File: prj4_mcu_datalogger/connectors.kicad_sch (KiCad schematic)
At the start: 4 parts, among them J1 Conn_01x04_Pin, J2 Conn_01x04_Pin, J3 Conn_01x09_Pin, J4 Conn_02x03_Odd_Even

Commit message: Associazione simboli/footprint
Feat: associati i simboli dei componenti con i relativi footprint
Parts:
- J1, J2: footprint (none) -> Connector_PinHeader_2.54mm:PinHeader_1x04_P2.54mm_Vertical
- J3: footprint (none) -> Connector_PinHeader_2.54mm:PinHeader_1x09_P2.54mm_Vertical
- J4: footprint (none) -> Connector_PinHeader_2.54mm:PinHeader_2x03_P2.54mm_Vertical
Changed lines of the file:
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@@
       (effects (font (size 1.27 1.27)))
     )
-    (property "Footprint" "" (at 121.92 73.66 0)
+    (property "Footprint" "Connector_PinHeader_2.54mm:PinHeader_1x04_P2.54mm_Vertical" (at 121.92 73.66 0)
       (effects (font (size 1.27 1.27)) hide)
     )
@@
       (effects (font (size 1.27 1.27)))
     )
-    (property "Footprint" "" (at 121.92 109.22 0)
+    (property "Footprint" "Connector_PinHeader_2.54mm:PinHeader_1x09_P2.54mm_Vertical" (at 121.92 109.22 0)
       (effects (font (size 1.27 1.27)) hide)
     )
@@
       (effects (font (size 1.27 1.27)))
     )
-    (property "Footprint" "" (at 165.1 109.22 0)
+    (property "Footprint" "Connector_PinHeader_2.54mm:PinHeader_2x03_P2.54mm_Vertical" (at 165.1 109.22 0)
       (effects (font (size 1.27 1.27)) hide)
     )
@@
       (effects (font (size 1.27 1.27)))
     )
-    (property "Footprint" "" (at 165.1 73.66 0)
+    (property "Footprint" "Connector_PinHeader_2.54mm:PinHeader_1x04_P2.54mm_Vertical" (at 165.1 73.66 0)
       (effects (font (size 1.27 1.27)) hide)
     )

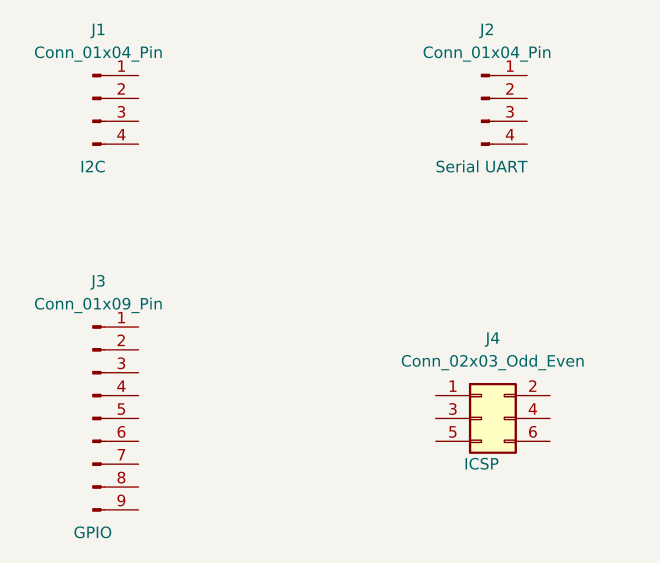
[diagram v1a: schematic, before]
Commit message: Completate le connessioni nello schematico
Feat: connessi tutti i pin in entrambi i fogli
Feat: effettuato ERC
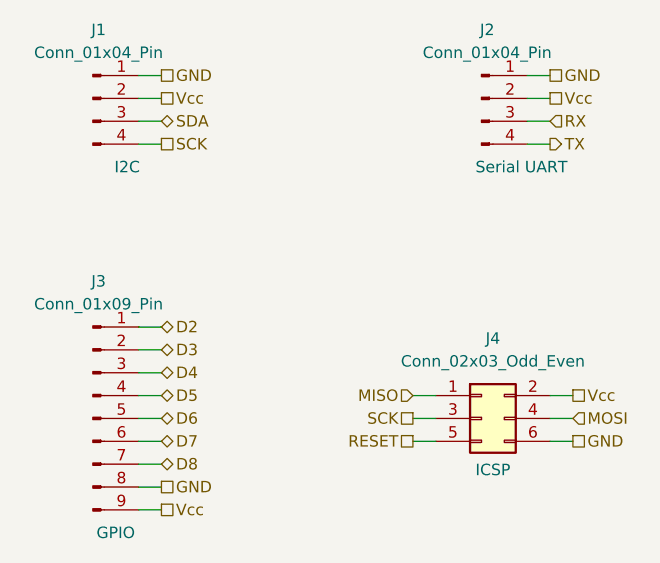
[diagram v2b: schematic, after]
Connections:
- net GND: now reaches J1.1 (Pin_1)
- net GND: now also J2.1 (Pin_1), J3.8 (Pin_8), J4.6 (Pin_6)
- net Vcc: now reaches J1.2 (Pin_2)
- net Vcc: now also J2.2 (Pin_2), J3.9 (Pin_9), J4.2 (Pin_2)
- net SDA: now reaches J1.3 (Pin_3)
- net SCK: now reaches J1.4 (Pin_4)
- net SCK: now also J4.3 (Pin_3)
- net D2: now reaches J3.1 (Pin_1)
- net D3: now reaches J3.2 (Pin_2)
- net D4: now reaches J3.3 (Pin_3)
- net D5: now reaches J3.4 (Pin_4)
- net D6: now reaches J3.5 (Pin_5)
- net D7: now reaches J3.6 (Pin_6)
- net D8: now reaches J3.7 (Pin_7)
- net MISO: now reaches J4.1 (Pin_1)
- net MOSI: now reaches J4.4 (Pin_4)
- net RESET: now reaches J4.5 (Pin_5)
- net RX: now reaches J2.3 (Pin_3)
- net TX: now reaches J2.4 (Pin_4)
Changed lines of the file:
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@@
 (kicad_sch (version 20230121) (generator eeschema)
   (paper "A4")
+  (wire (pts (xy 127 109.22) (xy 129.54 109.22))
+    (stroke (width 0) (type default))
+  )
+  (wire (pts (xy 127 78.74) (xy 129.54 78.74))
+    (stroke (width 0) (type default))
+  )
+  (wire (pts (xy 127 73.66) (xy 129.54 73.66))
+    (stroke (width 0) (type default))
+  )
+  (wire (pts (xy 170.18 78.74) (xy 172.72 78.74))
+    (stroke (width 0) (type default))
+  )
+  (wire (pts (xy 172.72 111.76) (xy 175.26 111.76))
+    (stroke (width 0) (type default))
+  )
+  (wire (pts (xy 170.18 71.12) (xy 172.72 71.12))
+    (stroke (width 0) (type default))
+  )
+  (wire (pts (xy 127 106.68) (xy 129.54 106.68))
+    (stroke (width 0) (type default))
+  )
+  (wire (pts (xy 127 76.2) (xy 129.54 76.2))
+    (stroke (width 0) (type default))
+  )
+  (wire (pts (xy 127 99.06) (xy 129.54 99.06))
+    (stroke (width 0) (type default))
+  )
+  (wire (pts (xy 127 116.84) (xy 129.54 116.84))
+    (stroke (width 0) (type default))
+  )
+  (wire (pts (xy 127 71.12) (xy 129.54 71.12))
+    (stroke (width 0) (type default))
+  )
+  (wire (pts (xy 157.48 111.76) (xy 160.02 111.76))
+    (stroke (width 0) (type default))
+  )
+  (wire (pts (xy 170.18 76.2) (xy 172.72 76.2))
+    (stroke (width 0) (type default))
+  )
+  (wire (pts (xy 157.48 109.22) (xy 160.02 109.22))
+    (stroke (width 0) (type default))
+  )
+  (wire (pts (xy 127 111.76) (xy 129.54 111.76))
+    (stroke (width 0) (type default))
+  )
+  (wire (pts (xy 127 119.38) (xy 129.54 119.38))
+    (stroke (width 0) (type default))
+  )
+  (wire (pts (xy 127 104.14) (xy 129.54 104.14))
+    (stroke (width 0) (type default))
+  )
+  (wire (pts (xy 172.72 106.68) (xy 175.26 106.68))
+    (stroke (width 0) (type default))
+  )
+  (wire (pts (xy 157.48 106.68) (xy 160.02 106.68))
+    (stroke (width 0) (type default))
+  )
+  (wire (pts (xy 127 114.3) (xy 129.54 114.3))
+    (stroke (width 0) (type default))
+  )
+  (wire (pts (xy 127 101.6) (xy 129.54 101.6))
+    (stroke (width 0) (type default))
+  )
+  (wire (pts (xy 172.72 109.22) (xy 175.26 109.22))
+    (stroke (width 0) (type default))
+  )
+  (wire (pts (xy 170.18 73.66) (xy 172.72 73.66))
+    (stroke (width 0) (type default))
+  )
+  (hierarchical_label "GND" (shape passive) (at 129.54 71.12 0) (fields_autoplaced)
+    (effects (font (size 1.27 1.27)) (justify left))
+  )
+  (hierarchical_label "GND" (shape passive) (at 175.26 111.76 0) (fields_autoplaced)
+    (effects (font (size 1.27 1.27)) (justify left))
+  )
+  (hierarchical_label "RX" (shape input) (at 172.72 76.2 0) (fields_autoplaced)
+    (effects (font (size 1.27 1.27)) (justify left))
+  )
+  (hierarchical_label "SCK" (shape passive) (at 129.54 78.74 0) (fields_autoplaced)
+    (effects (font (size 1.27 1.27)) (justify left))
+  )
+  (hierarchical_label "D3" (shape bidirectional) (at 129.54 101.6 0) (fields_autoplaced)
+    (effects (font (size 1.27 1.27)) (justify left))
+  )
+  (hierarchical_label "GND" (shape passive) (at 172.72 71.12 0) (fields_autoplaced)
+    (effects (font (size 1.27 1.27)) (justify left))
+  )
+  (hierarchical_label "D5" (shape bidirectional) (at 129.54 106.68 0) (fields_autoplaced)
+    (effects (font (size 1.27 1.27)) (justify left))
+  )
+  (hierarchical_label "Vcc" (shape passive) (at 175.26 106.68 0) (fields_autoplaced)
+    (effects (font (size 1.27 1.27)) (justify left))
+  )
+  (hierarchical_label "D8" (shape bidirectional) (at 129.54 114.3 0) (fields_autoplaced)
+    (effects (font (size 1.27 1.27)) (justify left))
+  )
+  (hierarchical_label "SCK" (shape passive) (at 157.48 109.22 180) (fields_autoplaced)
+    (effects (font (size 1.27 1.27)) (justify right))
+  )
+  (hierarchical_label "Vcc" (shape passive) (at 129.54 119.38 0) (fields_autoplaced)
+    (effects (font (size 1.27 1.27)) (justify left))
+  )
+  (hierarchical_label "GND" (shape passive) (at 129.54 116.84 0) (fields_autoplaced)
+    (effects (font (size 1.27 1.27)) (justify left))
+  )
+  (hierarchical_label "D7" (shape bidirectional) (at 129.54 111.76 0) (fields_autoplaced)
+    (effects (font (size 1.27 1.27)) (justify left))
+  )
+  (hierarchical_label "Vcc" (shape passive) (at 172.72 73.66 0) (fields_autoplaced)
+    (effects (font (size 1.27 1.27)) (justify left))
+  )
+  (hierarchical_label "MISO" (shape input) (at 157.48 106.68 180) (fields_autoplaced)
+    (effects (font (size 1.27 1.27)) (justify right))
+  )
+  (hierarchical_label "Vcc" (shape passive) (at 129.54 73.66 0) (fields_autoplaced)
+    (effects (font (size 1.27 1.27)) (justify left))
+  )
+  (hierarchical_label "D2" (shape bidirectional) (at 129.54 99.06 0) (fields_autoplaced)
+    (effects (font (size 1.27 1.27)) (justify left))
+  )
+  (hierarchical_label "D4" (shape bidirectional) (at 129.54 104.14 0) (fields_autoplaced)
+    (effects (font (size 1.27 1.27)) (justify left))
+  )
+  (hierarchical_label "SDA" (shape bidirectional) (at 129.54 76.2 0) (fields_autoplaced)
+    (effects (font (size 1.27 1.27)) (justify left))
+  )
+  (hierarchical_label "RESET" (shape passive) (at 157.48 111.76 180) (fields_autoplaced)
+    (effects (font (size 1.27 1.27)) (justify right))
+  )
+  (hierarchical_label "MOSI" (shape input) (at 175.26 109.22 0) (fields_autoplaced)
+    (effects (font (size 1.27 1.27)) (justify left))
+  )
+  (hierarchical_label "TX" (shape output) (at 172.72 78.74 0) (fields_autoplaced)
+    (effects (font (size 1.27 1.27)) (justify left))
+  )
+  (hierarchical_label "D6" (shape bidirectional) (at 129.54 109.22 0) (fields_autoplaced)
+    (effects (font (size 1.27 1.27)) (justify left))
+  )
   (symbol (lib_id "Connector:Conn_01x04_Pin") (at 121.92 73.66 0) (unit 1)
     (in_bom yes) (on_board yes) (dnp no)
@@
       (effects (font (size 1.27 1.27)) hide)
     )
-    (property "Purpose" "I2C" (at 121.92 81.28 0)
+    (property "Purpose" "I2C" (at 125.73 81.28 0)
       (effects (font (size 1.27 1.27)))
     )
@@
       (effects (font (size 1.27 1.27)) hide)
     )
-    (property "Purpose" "GPIO" (at 121.92 121.92 0)
+    (property "Purpose" "GPIO" (at 124.46 121.92 0)
       (effects (font (size 1.27 1.27)))
     )
@@
       (effects (font (size 1.27 1.27)) hide)
     )
-    (property "Purpose" "ICSP" (at 165.1 114.3 0)
+    (property "Purpose" "ICSP" (at 166.37 114.935 0)
       (effects (font (size 1.27 1.27)))
     )
@@
       (effects (font (size 1.27 1.27)) hide)
     )
-    (property "Purpose" "Serial UART" (at 165.1 81.28 0)
-      (effects (font (size 1.27 1.27)))
-    )
+    (property "Purpose" "Serial UART" (at 169.545 81.28 0)
+      (effects (font (size 1.27 1.27)))
+    )

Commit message: Correzione SCK
Fix: SCL era nominato SCK (erano in corto), ora sono separati
Fix: numerati i REF degli elementi grafici su Pcbnew
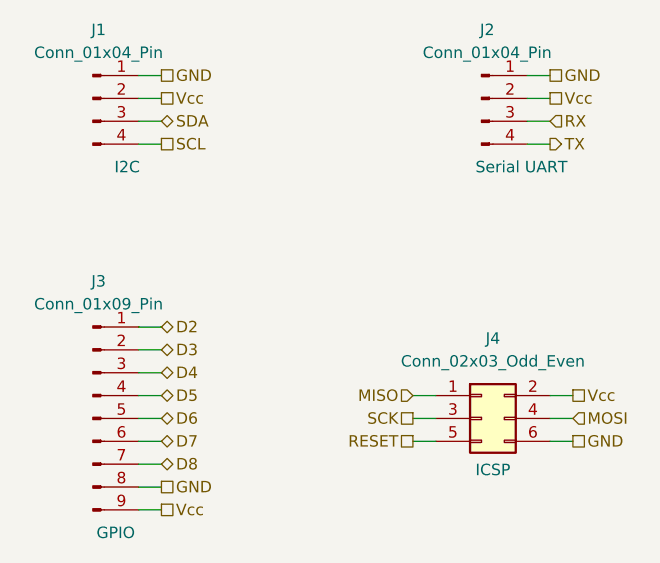
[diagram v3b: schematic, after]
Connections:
- net SCK: no longer J1.4 (Pin_4)
- new net SCL: J1.4 (Pin_4)
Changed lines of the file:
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@@
     (effects (font (size 1.27 1.27)) (justify left))
   )
-  (hierarchical_label "SCK" (shape passive) (at 129.54 78.74 0) (fields_autoplaced)
+  (hierarchical_label "SCL" (shape passive) (at 129.54 78.74 0) (fields_autoplaced)
     (effects (font (size 1.27 1.27)) (justify left))
   )
